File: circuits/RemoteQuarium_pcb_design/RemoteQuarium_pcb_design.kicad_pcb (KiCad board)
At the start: 2 copper layers, 99.1 x 53.3 mm, 37 parts, among them J1 Power_terminal, J10 LCD_pins, J11 Feeder_servo_pins, J12 ESP_pins, J13 PH_sensor_sockets, J14 Ph_sesnor-pins, J15 Power & D3-D4, J16 Reset_button_terminal, J2 ESP left side sockets, J3 ESP right side sockets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

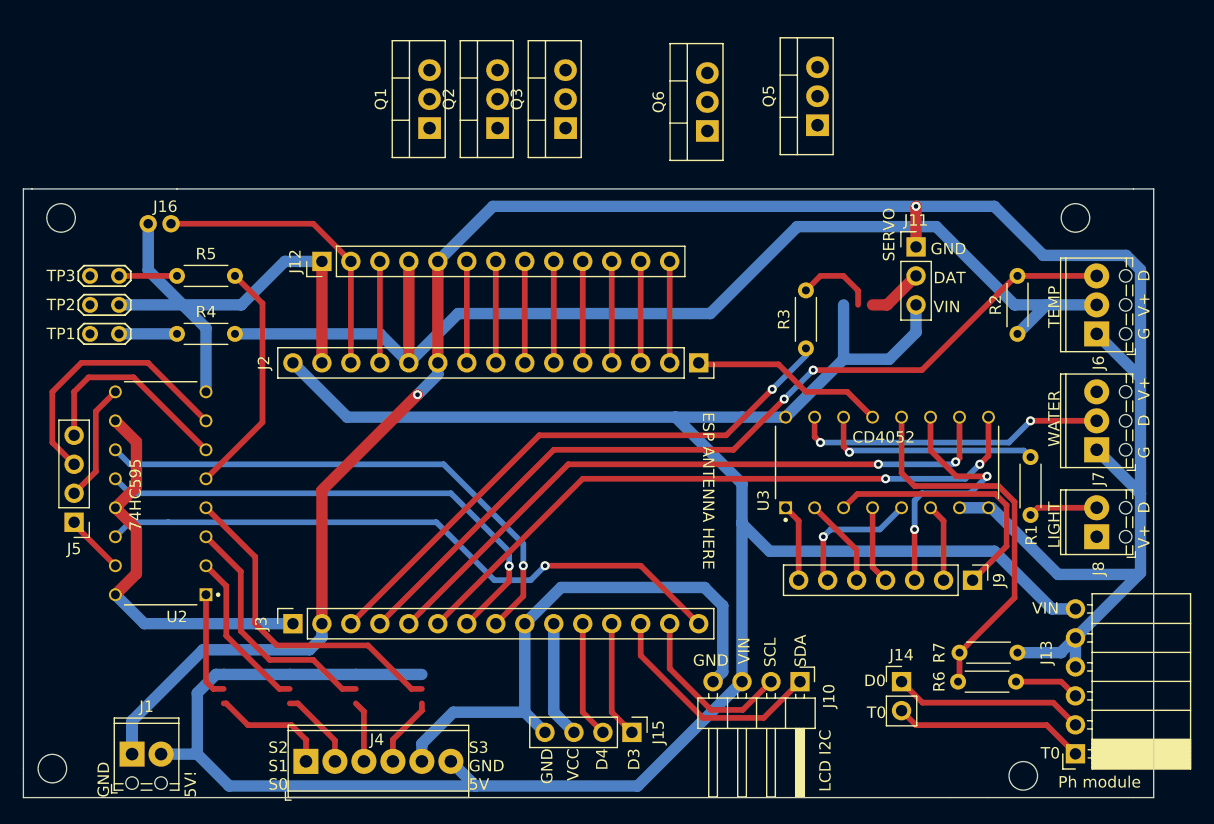
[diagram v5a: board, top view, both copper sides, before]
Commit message: Notifications are working, also fixed up the circuit a little. Added all notifications to switch in main
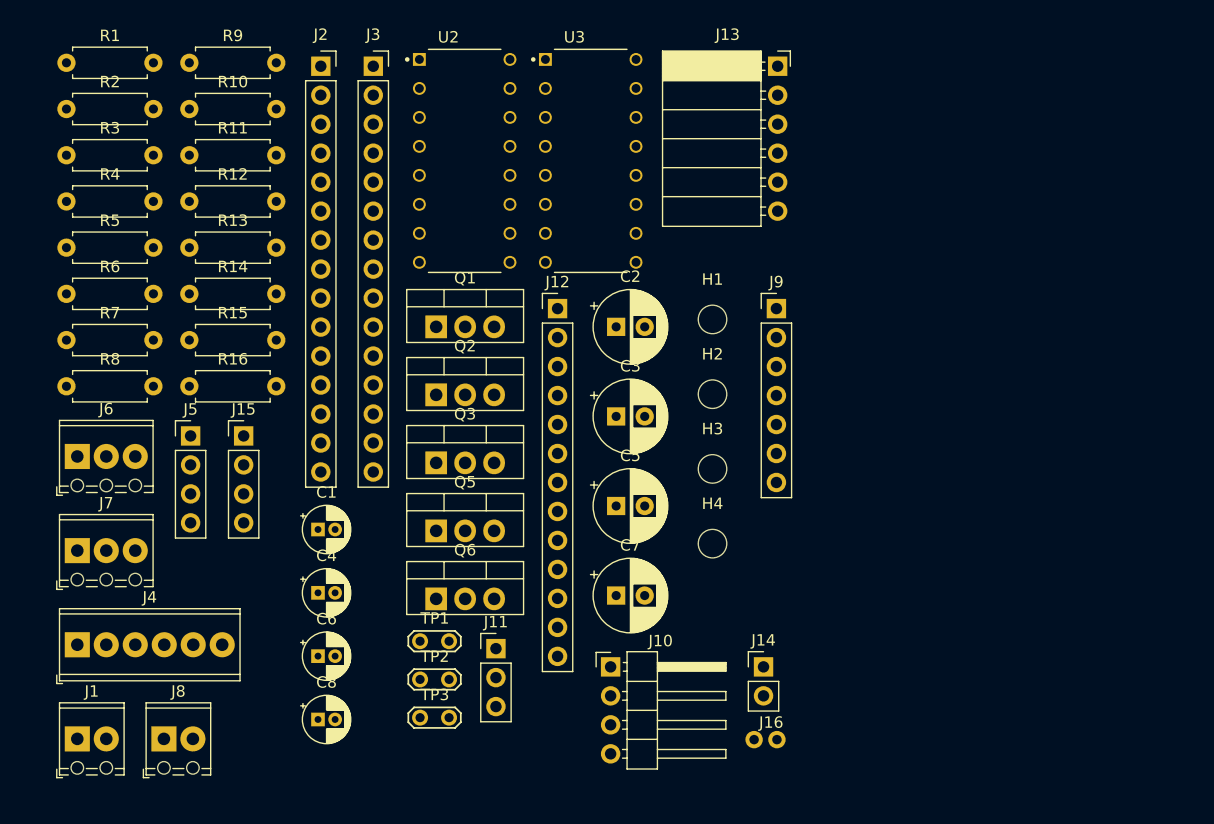
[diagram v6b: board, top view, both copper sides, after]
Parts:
- added C1: 1uF, Capacitor_THT:CP_Radial_D4.0mm_P1.50mm, F.Cu at (119.8, 103.5)
- added C2: 100uF, Capacitor_THT:CP_Radial_D6.3mm_P2.50mm, F.Cu at (145.9, 85.7)
- added C3: 100uF, Capacitor_THT:CP_Radial_D6.3mm_P2.50mm, F.Cu at (145.9, 93.6)
- added C4: 1uF, Capacitor_THT:CP_Radial_D4.0mm_P1.50mm, F.Cu at (119.8, 109.1)
- added C5: 100uF, Capacitor_THT:CP_Radial_D6.3mm_P2.50mm, F.Cu at (145.9, 101.4)
- added C6: 1uF, Capacitor_THT:CP_Radial_D4.0mm_P1.50mm, F.Cu at (119.8, 114.6)
- added C7: 100uF, Capacitor_THT:CP_Radial_D6.3mm_P2.50mm, F.Cu at (145.9, 109.3)
- added C8: 1uF, Capacitor_THT:CP_Radial_D4.0mm_P1.50mm, F.Cu at (119.8, 120.2)
- added R10: 220R, Resistor_THT:R_Axial_DIN0207_L6.3mm_D2.5mm_P7.62mm_Horizontal, F.Cu at (108.5, 66.7)
- added R11: 220R, Resistor_THT:R_Axial_DIN0207_L6.3mm_D2.5mm_P7.62mm_Horizontal, F.Cu at (108.5, 70.7)
- added R12: 10kR, Resistor_THT:R_Axial_DIN0207_L6.3mm_D2.5mm_P7.62mm_Horizontal, F.Cu at (108.5, 74.8)
- added R13: 10kR, Resistor_THT:R_Axial_DIN0207_L6.3mm_D2.5mm_P7.62mm_Horizontal, F.Cu at (108.5, 78.8)
- added R14: 10kR, Resistor_THT:R_Axial_DIN0207_L6.3mm_D2.5mm_P7.62mm_Horizontal, F.Cu at (108.5, 82.9)
- added R15: 10kR, Resistor_THT:R_Axial_DIN0207_L6.3mm_D2.5mm_P7.62mm_Horizontal, F.Cu at (108.5, 86.9)
- added R16: 10kR, Resistor_THT:R_Axial_DIN0207_L6.3mm_D2.5mm_P7.62mm_Horizontal, F.Cu at (108.5, 91.0)
- added R8: 220R, Resistor_THT:R_Axial_DIN0207_L6.3mm_D2.5mm_P7.62mm_Horizontal, F.Cu at (97.8, 91.0)
- added R9: 220R, Resistor_THT:R_Axial_DIN0207_L6.3mm_D2.5mm_P7.62mm_Horizontal, F.Cu at (108.5, 62.6)
- R1, R2, R4, R5, R6, R7: footprint Resistor_THT:R_Axial_DIN0204_L3.6mm_D1.6mm_P5.08mm_Horizontal -> Resistor_THT:R_Axial_DIN0207_L6.3mm_D2.5mm_P7.62mm_Horizontal
- R3: value 10kR -> 1kR; footprint Resistor_THT:R_Axial_DIN0204_L3.6mm_D1.6mm_P5.08mm_Horizontal -> Resistor_THT:R_Axial_DIN0207_L6.3mm_D2.5mm_P7.62mm_Horizontal
- moved R1 93.3 mm to (97.8, 62.6), turned to 0 degrees
- moved J6 90.0 mm to (98.7, 97.1), turned to 0 degrees
- moved J7 89.8 mm to (98.7, 105.4), turned to 0 degrees
- moved R7 87.7 mm to (97.8, 86.9), turned to 0 degrees
- moved R2 85.6 mm to (97.8, 66.7), turned to 0 degrees
- moved R6 85.2 mm to (97.8, 82.9)
- moved J8 83.6 mm to (106.3, 121.9), turned to 0 degrees
- moved J16 69.7 mm to (158.0, 121.9)
- moved R3 67.0 mm to (97.8, 70.7), turned to 0 degrees
- moved J13 65.7 mm to (160.1, 62.9), turned to 0 degrees
- moved H3 61.2 mm to (154.4, 98.2), turned to 0 degrees
- moved H4 61.1 mm to (154.4, 104.7)
- moved J11 50.9 mm to (135.4, 113.9)
- moved J3 49.4 mm to (124.6, 62.9), turned to 0 degrees
- moved Q5 48.8 mm to (130.2, 103.6), turned to 0 degrees
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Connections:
- Q1 pad 1: /S1 -> Net-(Q1-G)
- Q2 pad 1: /S2 -> Net-(Q2-G)
- Q3 pad 1: /S3 -> Net-(Q3-G)
- Q6 pad 1: /S0 -> Net-(Q6-G)
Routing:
- net /GND: track 297.4 -> 0.00 mm, vias 2 -> 0
- net /VIN: track 209.5 -> 0.00 mm
- net /VCC: track 142.0 -> 0.00 mm
- net /RX: track 75.4 -> 0.00 mm, vias 2 -> 0
- net /D8: track 57.9 -> 0.00 mm, vias 2 -> 0
- net /D7: track 57.7 -> 0.00 mm, vias 2 -> 0
- net /D0: track 56.4 -> 0.00 mm, vias 1 -> 0
- net /TX: track 50.2 -> 0.00 mm, vias 1 -> 0
- net /D5: track 47.2 -> 0.00 mm, vias 1 -> 0
- net /D6: track 45.0 -> 0.00 mm, vias 1 -> 0
- net /P0R: track 33.6 -> 0.00 mm
- net /S3: track 28.9 -> 0.00 mm
- net /WATER_DAT: track 27.4 -> 0.00 mm, vias 2 -> 0
- net /RST: track 26.0 -> 0.00 mm
- net /QH: track 23.8 -> 0.00 mm
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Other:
- board outline removed
- board text removed: "5V!"
- board text removed: "74HC595"
- board text removed: "CD4052"
- board text removed: "D"
- board text removed: "D0"
- board text removed: "D3"
- board text removed: "D4"
- board text removed: "DAT"
- board text removed: "ESP ANTENNA HERE"
- board text removed: "ESP port and sensor interface board for ATC system v1.0"
- board text removed: "G"
- board text removed: "GND"
- board text removed: "LCD I2C"
- board text removed: "LIGHT"
- board text removed: "Ph module"
- board text removed: "S2 S1 S0"
- board text removed: "S3 GND 5V"
- board text removed: "SCL"
- board text removed: "SDA"
- board text removed: "SERVO"
- board text removed: "T0"
- board text removed: "TEMP"
- board text removed: "V+"
- board text removed: "VCC"
- board text removed: "VIN"
- board text removed: "WATER"

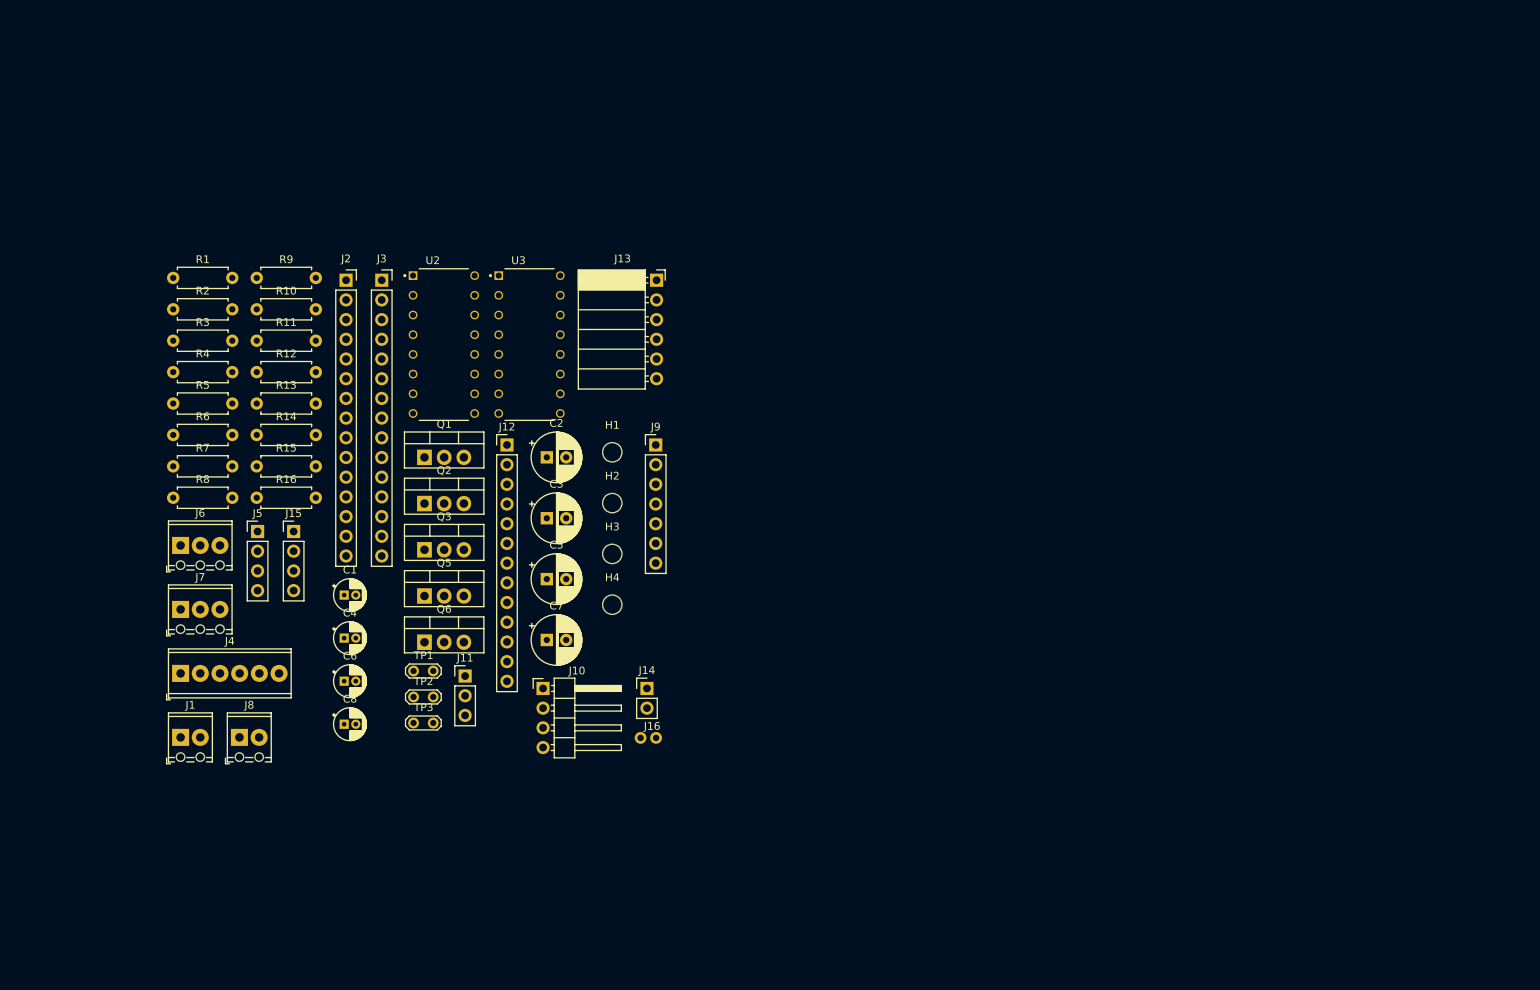
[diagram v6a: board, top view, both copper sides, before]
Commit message: Removed cleaning and waterchange from app since it won't be implemented and made the level shifter working
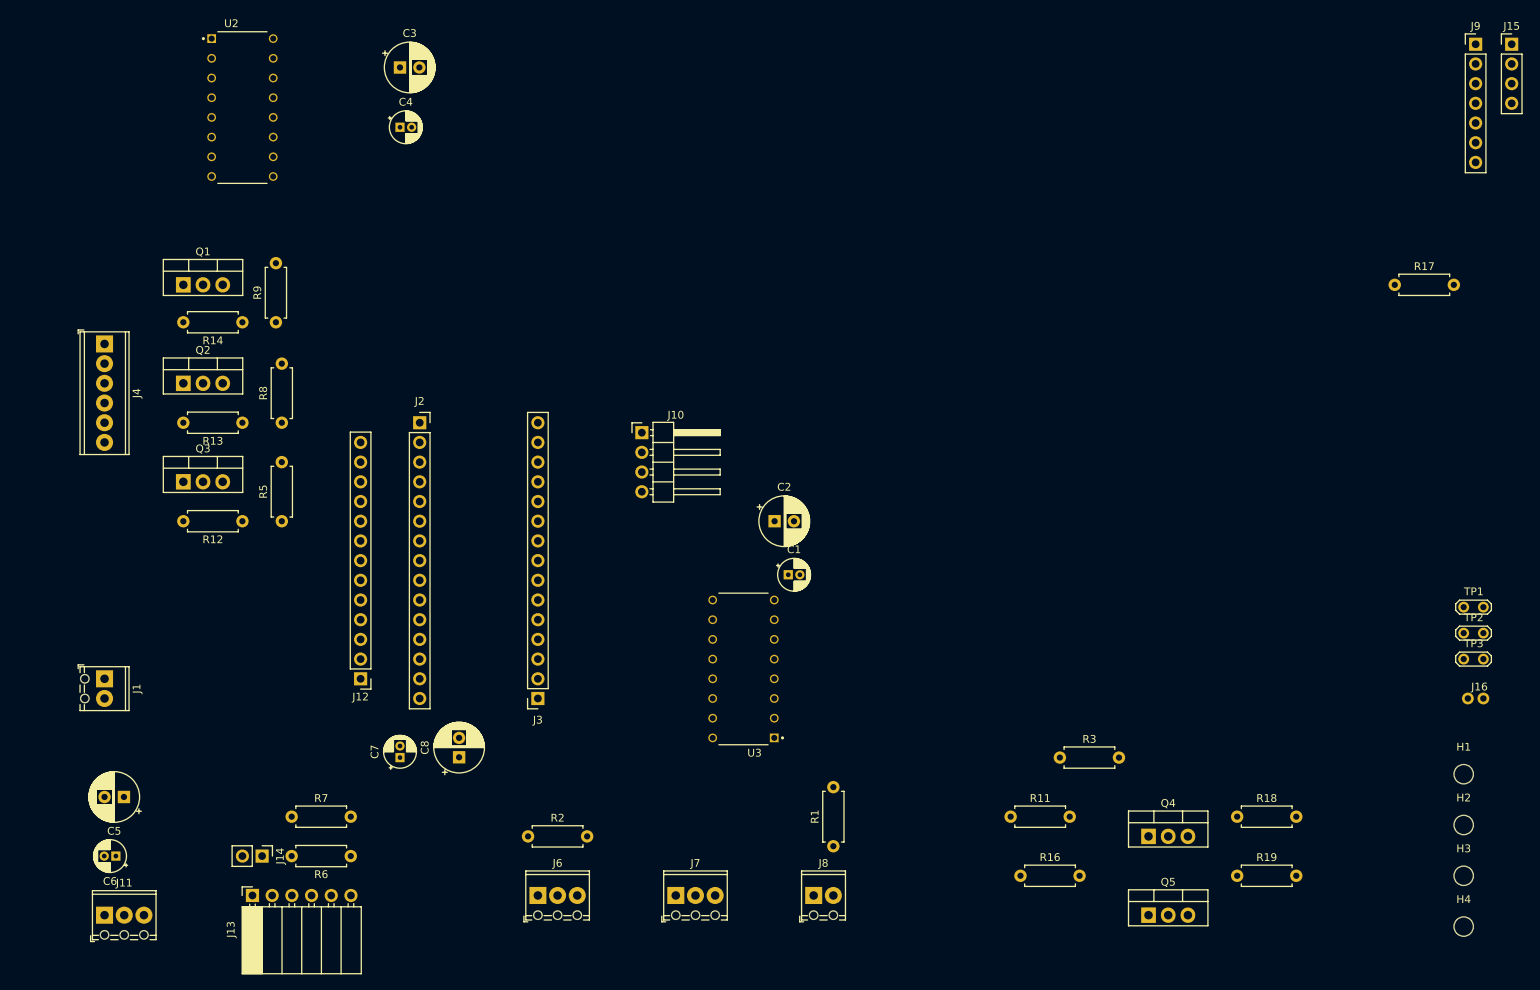
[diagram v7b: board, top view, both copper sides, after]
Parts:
- removed J5: SREG_pins, Connector_PinHeader_2.54mm:PinHeader_1x04_P2.54mm_Vertical
- removed Q6: IRLZ34N, Package_TO_SOT_THT:TO-220-3_Vertical
- removed R10: 220R, Resistor_THT:R_Axial_DIN0207_L6.3mm_D2.5mm_P7.62mm_Horizontal
- removed R15: 10kR, Resistor_THT:R_Axial_DIN0207_L6.3mm_D2.5mm_P7.62mm_Horizontal
- removed R4: 470R, Resistor_THT:R_Axial_DIN0207_L6.3mm_D2.5mm_P7.62mm_Horizontal
- added Q4: IRLZ34N, Package_TO_SOT_THT:TO-220-3_Vertical, F.Cu at (223.5, 134.6)
- added R17: 470R, Resistor_THT:R_Axial_DIN0207_L6.3mm_D2.5mm_P7.62mm_Horizontal, F.Cu at (255.3, 63.5)
- added R18: 100k, Resistor_THT:R_Axial_DIN0207_L6.3mm_D2.5mm_P7.62mm_Horizontal, F.Cu at (234.9, 132.1)
- added R19: 100k, Resistor_THT:R_Axial_DIN0207_L6.3mm_D2.5mm_P7.62mm_Horizontal, F.Cu at (234.9, 139.7)
- C1, C4, C6: value 1uF -> 0.1uF
- C2, C3, C5: value 100uF -> 10uF
- C7: value 100uF -> 0.1uF; footprint Capacitor_THT:CP_Radial_D6.3mm_P2.50mm -> Capacitor_THT:CP_Radial_D4.0mm_P1.50mm
- C8: value 1uF -> 10uF; footprint Capacitor_THT:CP_Radial_D4.0mm_P1.50mm -> Capacitor_THT:CP_Radial_D6.3mm_P2.50mm
- J11: value Feeder_servo_pins -> Servo pins; footprint Connector_PinHeader_2.54mm:PinHeader_1x03_P2.54mm_Vertical -> TerminalBlock_Phoenix:TerminalBlock_Phoenix_MPT-0,5-3-2.54_1x03_P2.54mm_Horizontal
- J15: value Power & D3-D4 -> Power & RX-TX
- R11: value 220R -> 4.7k
- R12, R13, R14: value 10kR -> 4.7kR
- R16: value 10kR -> 1k
- R3: value 1kR -> 4.7k
- R5: value 470R -> 10kR
- R8, R9: value 220R -> 10kR
- TP2: value LED_common_cat -> LED_common_an
- moved J15 169.2 mm to (270.4, 32.5)
- moved TP1 135.7 mm to (264.2, 105.1)
- moved TP2 135.7 mm to (264.2, 108.4)
- moved TP3 135.7 mm to (264.2, 111.8)
- moved R3 126.3 mm to (212.1, 124.5)
- moved J9 117.7 mm to (265.7, 32.5)
- moved H2 117.4 mm to (264.2, 133.2)
- moved H1 117.4 mm to (264.2, 126.6)
- moved H3 117.4 mm to (264.2, 139.7)
- moved H4 117.4 mm to (264.2, 146.2)
- moved R11 115.0 mm to (205.7, 132.1)
- moved R1 112.3 mm to (182.9, 135.9), turned to 90 degrees
- moved R16 109.9 mm to (207.0, 139.7)
- moved J16 106.8 mm to (264.7, 116.8)
- moved Q5 102.0 mm to (223.5, 144.8)
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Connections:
- net /S15V renamed Net-(J4-Pin_2)
- net /S25V renamed Net-(J4-Pin_3)
- net /S35V renamed Net-(J4-Pin_4)
- C1 pad 1: /VIN -> Earth
- C1 pad 2: /GND -> /VIN
- C2 pad 1: /VIN -> Earth
- C2 pad 2: /GND -> /VIN
- C3 pad 1: /GND -> Earth
- C4 pad 1: /GND -> Earth
- C5 pad 2: /GND -> Earth
- C6 pad 2: /GND -> Earth
- C7 pad 1: /GND -> Earth
- C8 pad 1: /GND -> Earth
- J1 pad 1: /GND -> Earth
- J10 pad 4: /GND -> Earth
- J11 pad 1: /GND -> Earth
- J11 pad 2: /TX5V -> /VIN
- J11 pad 3: /VIN -> /D35V
- J12 pad 1: /GND -> Earth
- J12 pad 5: /GND -> Earth
- J13 pad 4: /GND -> Earth
- J13 pad 5: /GND -> Earth
- J15 pad 1: /D3 -> /TX
- J15 pad 2: /D4 -> /RX
- J15 pad 4: /GND -> Earth
- J16 pad 2: /GND -> Earth
- J2 pad 10: /GND -> Earth
- J2 pad 14: /GND -> Earth
- J3 pad 2: /GND -> Earth
- J3 pad 9: /GND -> Earth
- J4 pad 1: /S05V -> Earth
- J4 pad 5: /GND -> Earth
- J6 pad 1: /GND -> Earth
- J6 pad 3: /RX -> /D4
- J7 pad 1: /GND -> Earth
- Q1 pad 3: /VIN -> Earth
- Q2 pad 3: /VIN -> Earth
- Q3 pad 3: /VIN -> Earth
- Q5 pad 1: /TXR -> Net-(Q4-D)
- Q5 pad 2: /VIN -> /D35V
- Q5 pad 3: /TX5V -> Earth
- R1 pad 2: /LIGHT_DATR -> Earth
- R11 pad 1: Net-(Q6-G) -> /VIN
- R11 pad 2: /S0 -> Net-(Q4-D)
- R12 pad 1: /GND -> /S0
- R12 pad 2: Net-(Q6-G) -> Net-(Q3-G)
- R13 pad 1: /GND -> /S1
- R13 pad 2: Net-(Q1-G) -> Net-(Q2-G)
- R14 pad 1: /GND -> /S2
- R14 pad 2: Net-(Q2-G) -> Net-(Q1-G)
- R16 pad 1: /GND -> /VIN
- R16 pad 2: /TXR -> /D35V
- R2 pad 2: /RX -> /D4
- R3 pad 1: /TX -> /D3
- R3 pad 2: /TXR -> Net-(Q4-G)
- R5 pad 1: /R_LEDR -> /S0
- R5 pad 2: /R_LED -> Earth
- R7 pad 1: /GND -> Earth
- R8 pad 1: Net-(Q2-G) -> /S1
- R8 pad 2: /S2 -> Earth
- R9 pad 1: Net-(Q3-G) -> /S2
- R9 pad 2: /S3 -> Earth
- TP1 pad 1: /VCCR -> Earth
- TP2 pad 1: /GND -> /VCCR
- TP3 pad 1: /R_LEDR -> /R_LED
- U2 pad 13: /VCC -> Earth
- U2 pad 15: /QA -> Earth
- U2 pad 4: /S3 -> Earth
- U2 pad 6: /QG -> Earth
- U2 pad 7: /QH -> Earth
- U2 pad 8: /GND -> Earth
- U2 pad 9: /QH' -> Earth
- U3 pad 14: /LIGHT_DATR -> /LIGHT_DAT
- U3 pad 7: /GND -> Earth
- U3 pad 8: /GND -> Earth
